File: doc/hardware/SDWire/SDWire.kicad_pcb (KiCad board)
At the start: 4 copper layers, 21.6 x 48.4 mm, 80 parts, among them J1 usd-plug, J2 uSD Socket, P1 USB_OTG_MICRO_USB, Q3 MMBT4403LT1, Q4 MMBT4403LT1, U1 USB2640-HZH-02, U2 SPX3819M5, U3 FT200XD, U4 MC74HC1G04DTT1G, U5 TS3A27518EPWR, Y1 24MHz

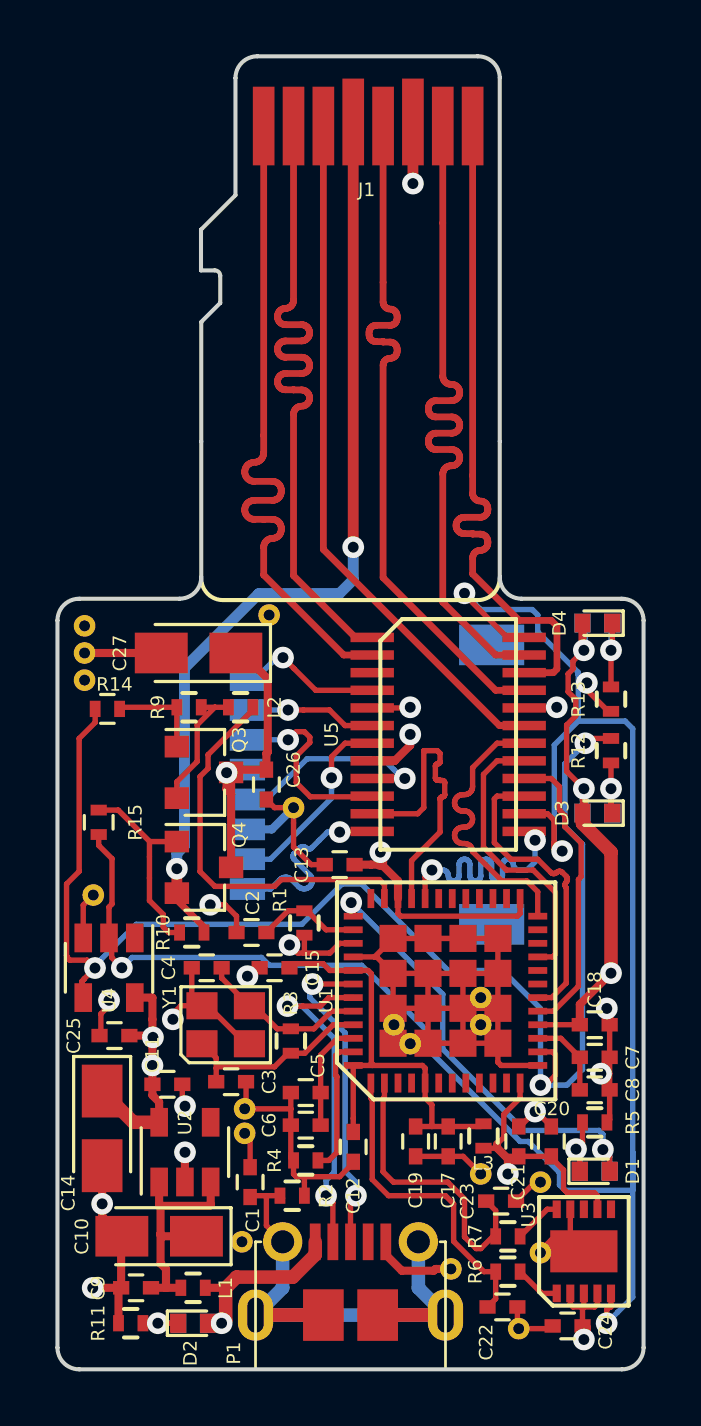
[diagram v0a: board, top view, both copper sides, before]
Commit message: Add EEPROM to SDWire device
EEPROM is used to store unique serial number for mass storage
reader in order to distinguish them in one USB host machine.

Change-Id: I45e7371c2a41f0804c17b799591ab44a722c4872
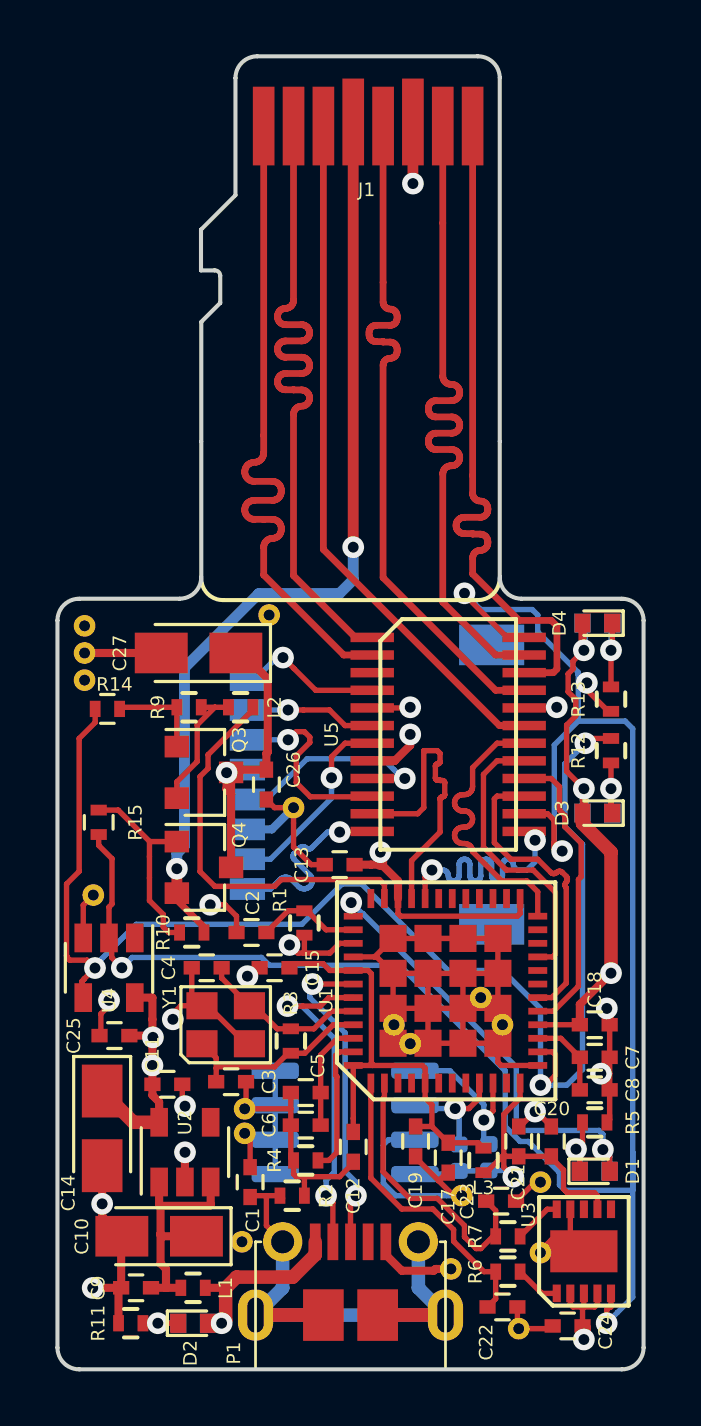
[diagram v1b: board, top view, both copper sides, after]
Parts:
- added R16: 10K, Resistor_SMD:R_0402_1005Metric, B.Cu at (151.2, 125.3)
- added R8: 10K, Resistor_SMD:R_0402_1005Metric, B.Cu at (152.3, 125.3)
- added U6: AT24CS02-SSHM, Package_SO:SO-8_3.9x4.9mm_P1.27mm, B.Cu at (147.0, 124.0)
- moved REF** 1.06 mm to (151.3, 126.7)
- moved L3 0.90 mm to (152.1, 125.4)
- moved REF** 0.80 mm to (152.8, 120.4)
- moved C17 0.60 mm to (150.8, 125.3)
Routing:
- net GND: track 102.7 -> 114.8 mm
- net Net-(R8-Pad2): track 0.00 -> 6.09 mm, vias 0 -> 1
- net Net-(R16-Pad2): track 0.00 -> 4.52 mm, vias 0 -> 1
- net +3V3: track 123.2 -> 126.7 mm
- net /SOCKET_SEL: track 76.8 -> 77.6 mm
- net /USB_B+: track 11.1 -> 10.5 mm
- net /USB_B-: track 11.8 -> 11.2 mm
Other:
- board text added: "SDWire v1.4"
- board text removed: "SDWire v1.3"

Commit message: Update assembly layer
Change-Id: I6dcabfdd0364e7ee87c664ed7b3d73991db7c9f6
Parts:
- D6: value OSB50402C1E -> BLUE
